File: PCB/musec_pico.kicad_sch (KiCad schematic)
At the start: 44 parts, among them SW1 SW_DIP_x01, SW2 SW_DIP_x01, SW3 SW_DIP_x01, SW4 SW_DIP_x01, SW5 SW_DIP_x01, SW6 SW_DIP_x01, SW7 SW_DIP_x01, U1 PiPico, U3 TMAG5273, U4 TMAG5273, U7 TMAG5273, U8 TMAG5273, U9 TMAG5273

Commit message: PCB progress 70%
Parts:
- added JA1, JA2, JA3, JA4, JA5, JB1, JB2, JB3, JB4, JB5: Conn_01x04, musec_pico:SH1.0_4P_Solder_Combo, symbol Connector_Generic:Conn_01x04
- U3, U4, U7, U8, U9: footprint Package_TO_SOT_SMD:TSOT-23-6_HandSoldering -> Package_TO_SOT_SMD:SOT-23-6
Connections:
- net SCL0 is gone; now on net SCL: U1.2 (GPIO1)
- net SDA0 is gone; now on net SDA: U1.1 (GPIO0)
- net +3V3: no longer C1.1, C2.1, C3.1, C4.1, C5.1
- net GND: now also U3.2 (GND), U3.3 (TEST), U4.2 (GND), U4.3 (TEST), U7.2 (GND), U7.3 (TEST), U8.2 (GND), U8.3 (TEST), U9.2 (GND), U9.3 (TEST), JA1.2 (Pin_2), JA2.2 (Pin_2), JA3.2 (Pin_2), JA4.2 (Pin_2), JA5.2 (Pin_2), JB1.2 (Pin_2), JB2.2 (Pin_2), JB3.2 (Pin_2), JB4.2 (Pin_2), JB5.2 (Pin_2)
- net VB1: now also C1.1, U1.17 (GPIO13), JA1.1 (Pin_1), JB1.1 (Pin_1)
- net VB2: now also C2.1, U1.16 (GPIO12), JA2.1 (Pin_1), JB2.1 (Pin_1)
- net VB3: now also C3.1, U1.15 (GPIO11), JA3.1 (Pin_1), JB3.1 (Pin_1)
- net VB4: now also C4.1, U1.14 (GPIO10), JA4.1 (Pin_1), JB4.1 (Pin_1)
- net VB5: now also C5.1, U1.12 (GPIO9), JA5.1 (Pin_1), JB5.1 (Pin_1)
- net SCL: now reaches U3.1 (SCL), U4.1 (SCL), U7.1 (SCL), U8.1 (SCL), U8.6 (SDA), U9.1 (SCL)
- net SCL: now also JA1.4 (Pin_4), JA2.4 (Pin_4), JA3.4 (Pin_4), JA4.4 (Pin_4), JA5.4 (Pin_4), JB1.4 (Pin_4), JB2.4 (Pin_4), JB3.4 (Pin_4), JB4.4 (Pin_4), JB5.4 (Pin_4)
- net SDA: now reaches U3.6 (SDA), U4.6 (SDA), U7.6 (SDA), U9.6 (SDA)
- net SDA: now also JA1.3 (Pin_3), JA2.3 (Pin_3), JA3.3 (Pin_3), JA4.3 (Pin_3), JA5.3 (Pin_3), JB1.3 (Pin_3), JB2.3 (Pin_3), JB3.3 (Pin_3), JB4.3 (Pin_3), JB5.3 (Pin_3)
- net AUDIO_L: no longer names the net of U1.11 (GPIO8)
- net AUDIO_R: no longer names the net of U1.9 (GPIO6)
- no-connect marks 21 -> 19

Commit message: PCB almost done (95%)
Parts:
- renumbered U8 to U4, U4 to U5, U9 to U6
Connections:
- net GND: now also D17.G (VSS), D18.G (VSS), D19.G (VSS), D20.G (VSS), D21.G (VSS), D22.G (VSS)
- net SCL: no longer U4.6 (SDA)
- net SDA: now also U4.6 (SDA)
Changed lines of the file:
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@@
 	)
 	(junction
-		(at 267.335 41.275)
-		(diameter 0)
-		(color 0 0 0 0)
-	)
-	(junction
 		(at 158.75 170.18)
 		(diameter 0)
@@
 	)
 	(junction
+		(at 267.335 39.37)
+		(diameter 0)
+		(color 0 0 0 0)
+	)
+	(junction
 		(at 171.45 185.42)
 		(diameter 0)
@@
 	)
 	(junction
+		(at 133.35 214.63)
+		(diameter 0)
+		(color 0 0 0 0)
+	)
+	(junction
 		(at 234.95 170.18)
 		(diameter 0)
@@
 	(wire
 		(pts
-			(xy 267.335 87.63) (xy 267.335 41.275)
+			(xy 267.335 39.37) (xy 267.335 87.63)
 		)
 		(stroke
@@
 	(wire
 		(pts
-			(xy 271.78 87.63) (xy 267.335 87.63)
-		)
-		(stroke
-			(width 0)
-			(type default)
-		)
-	)
-	(wire
-		(pts
 			(xy 56.515 193.04) (xy 56.515 207.01)
 		)
@@
 	(wire
 		(pts
-			(xy 233.045 39.37) (xy 280.67 39.37)
+			(xy 233.045 39.37) (xy 267.335 39.37)
 		)
 		(stroke
@@
 	(wire
 		(pts
+			(xy 267.335 39.37) (xy 280.67 39.37)
+		)
+		(stroke
+			(width 0)
+			(type default)
+		)
+	)
+	(wire
+		(pts
 			(xy 340.995 141.605) (xy 340.995 153.67)
 		)
@@
 	(wire
 		(pts
+			(xy 267.335 87.63) (xy 271.78 87.63)
+		)
+		(stroke
+			(width 0)
+			(type default)
+		)
+	)
+	(wire
+		(pts
 			(xy 82.55 170.18) (xy 95.25 170.18)
 		)
@@
 	(wire
 		(pts
-			(xy 234.95 41.275) (xy 267.335 41.275)
-		)
-		(stroke
-			(width 0)
-			(type default)
-		)
-	)
-	(wire
-		(pts
 			(xy 82.55 214.63) (xy 95.25 214.63)
 		)
@@
 	(wire
 		(pts
-			(xy 267.335 41.275) (xy 269.24 41.275)
+			(xy 234.95 41.275) (xy 269.24 41.275)
 		)
 		(stroke
@@
 		(on_board yes)
 		(dnp no)
-		(property "Reference" "U9"
+		(property "Reference" "U6"
 			(at 318.135 79.375 0)
 			(effects
@@
 			(project "musec_pico"
 				(path "/2e3f5573-c264-4a8b-a2f0-0e6473d39aad"
-					(reference "U9")
+					(reference "U6")
 					(unit 1)
 				)
@@
 		(on_board yes)
 		(dnp no)
-		(property "Reference" "U8"
+		(property "Reference" "U4"
 			(at 274.955 78.74 0)
 			(effects
@@
 			(project "musec_pico"
 				(path "/2e3f5573-c264-4a8b-a2f0-0e6473d39aad"
-					(reference "U8")
+					(reference "U4")
 					(unit 1)
 				)
@@
 		(on_board yes)
 		(dnp no)
-		(property "Reference" "U4"
+		(property "Reference" "U5"
 			(at 288.925 52.07 0)
 			(effects
@@
 			(project "musec_pico"
 				(path "/2e3f5573-c264-4a8b-a2f0-0e6473d39aad"
-					(reference "U4")
+					(reference "U5")
 					(unit 1)
 				)
@@
 					(unit 1)
 				)
+			)
+		)
+	)
+	(symbol
+		(lib_id "power:GND")
+		(at 133.35 214.63 0)
+		(unit 1)
+		(exclude_from_sim no)
+		(in_bom yes)
+		(on_board yes)
+		(dnp no)
+		(property "Reference" "#PWR02"
+			(at 133.35 220.98 0)
+			(effects
+				(font
+					(size 1.27 1.27)
+				)
+				(hide yes)
+			)
+		)
+		(property "Value" "GND"
+			(at 133.35 218.44 0)
+			(effects
+				(font
+					(size 1.27 1.27)
+				)
+			)
+		)
+		(property "Footprint" ""
+			(at 133.35 214.63 0)
+			(effects
+				(font
+					(size 1.27 1.27)
+				)
+				(hide yes)
+			)
+		)
+		(property "Datasheet" ""
+			(at 133.35 214.63 0)
+			(effects
+				(font
+					(size 1.27 1.27)
+				)
+				(hide yes)
+			)
+		)
+		(property "Description" ""
+			(at 133.35 214.63 0)
+			(effects
+				(font
+					(size 1.27 1.27)
+				)
+				(hide yes)
+			)
+		)
+		(pin "1"
+		)
+		(instances
+			(project "musec_pico"
+				(path "/2e3f5573-c264-4a8b-a2f0-0e6473d39aad"
+					(reference "#PWR02")
+					(unit 1)
+				)

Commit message: PCB v1.0
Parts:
- added C10, C6, C7, C8, C9: 0.1uF, Capacitor_SMD:C_0603_1608Metric_Pad1.08x0.95mm_HandSolder, symbol Device:C
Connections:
- net +5V: now also C10.1, C6.1, C7.1, C8.1, C9.1
- net GND: now also C10.2, C6.2, C7.2, C8.2, C9.2

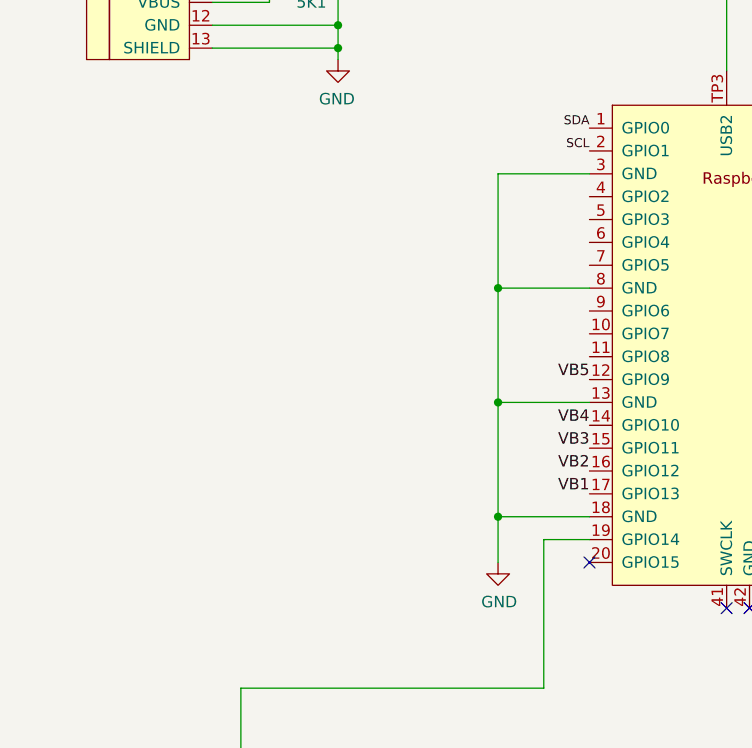
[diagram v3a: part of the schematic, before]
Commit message: PCB v1.1 to support pedal
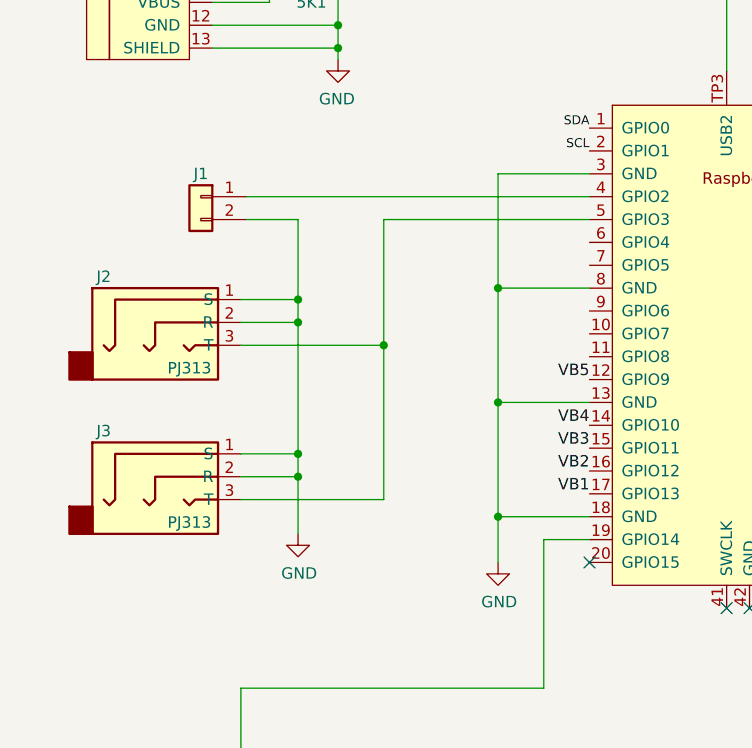
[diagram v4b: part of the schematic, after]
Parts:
- added J1: Conn_01x02, musec_pico:Solder_2P, symbol Connector_Generic:Conn_01x02
- added J2, J3: PJ313, musec_pico:PJ313, symbol musec_pico:PJ313
- U3, U4, U5, U6, U7: footprint Package_TO_SOT_SMD:SOT-23-6 -> Package_TO_SOT_SMD:TSOT-23-6_HandSoldering
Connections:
- net GND: now also J1.2 (Pin_2), J2.1 (S), J2.2 (R), J3.1 (S), J3.2 (R)
- net at U1.4 (GPIO2): now also J1.1 (Pin_1)
- net at U1.5 (GPIO3): now also J2.3 (T), J3.3 (T)

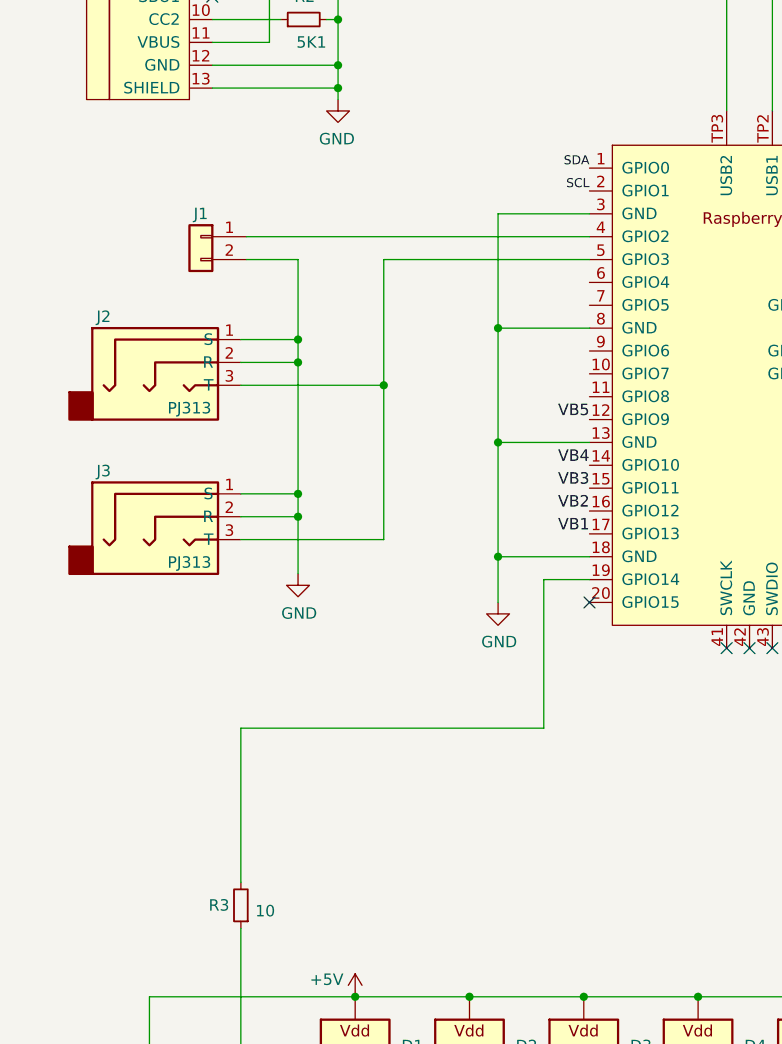
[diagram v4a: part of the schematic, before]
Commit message: PCB v1.2 (internal pedal connector and light)
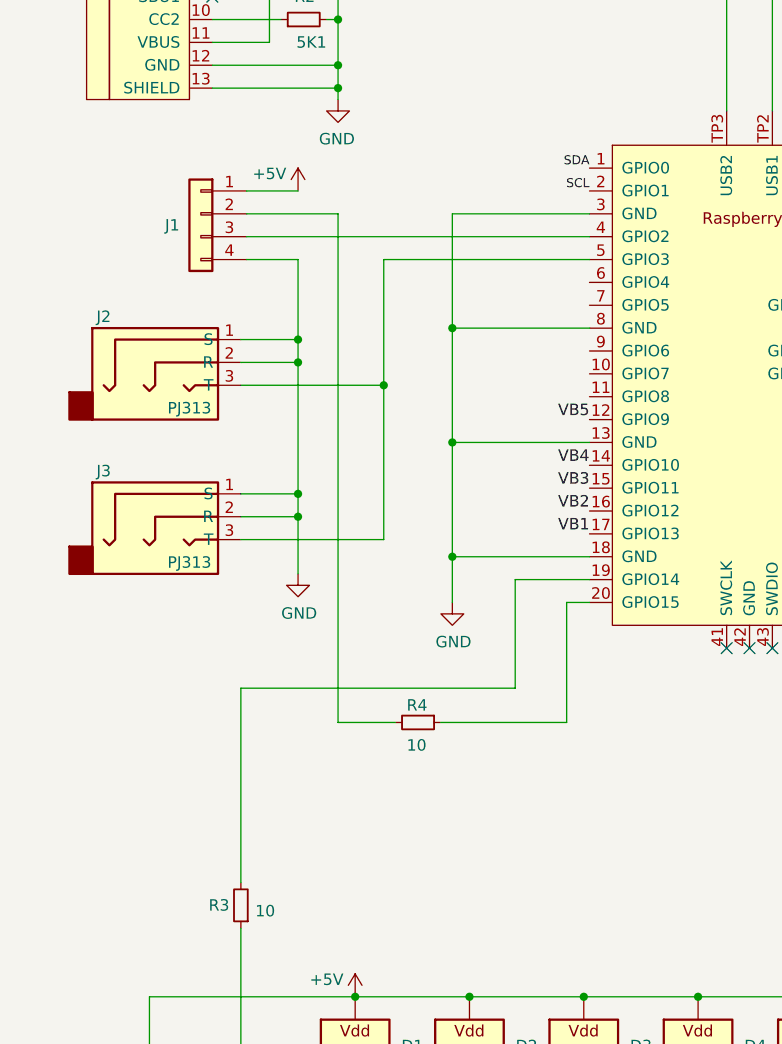
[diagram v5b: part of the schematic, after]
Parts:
- removed J1: Conn_01x02, musec_pico:Solder_2P, symbol Connector_Generic:Conn_01x02
- added J1: Pedal, musec_pico:SH1.0_4P_Solder_Combo, symbol Connector_Generic:Conn_01x04
- added R4: 10, Resistor_SMD:R_0603_1608Metric, symbol Device:R_Small
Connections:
- net +5V: now also J1.1 (Pin_1)
- net GND: now also J1.4 (Pin_4)
- net at U1.20 (GPIO15): now also R4.1
- net at U1.4 (GPIO2): now also J1.3 (Pin_3)
- new net: J1.2 (Pin_2), R4.2
- no-connect marks 19 -> 18
